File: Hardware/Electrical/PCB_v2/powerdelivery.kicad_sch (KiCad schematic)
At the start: 28 parts, among them J2 USB_C_Receptacle_USB2.0_16P, Q1 Q_PMOS, Q2 Q_PMOS, Q3 Q_PMOS, Q4 Q_PMOS, U2 TPD2EUSB30, U3 CYPD3177-24LQ

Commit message: Components placed
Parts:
- removed C14: 0.1 uF, Capacitor_SMD:C_0603_1608Metric, symbol Device:C
- C10, C13, C8, C9: value 0.1 uF -> 100nF; *LCSC Part Number (none) -> C14663; Manufacturer Würth Elektronik -> (none)
- C11, C12, C6, C7: *LCSC Part Number (none) -> C1848; Manufacturer YAGEO -> (none)
- D2: footprint (none) -> Diode_SMD:D_SOD-323
- J2: Manufacturer SHOU HAN -> (none); now not fitted
- Q1, Q2, Q3, Q4: *LCSC Part Number (none) -> C554002; Manufacturer Vishay Siliconix -> (none)
- R10, R8: footprint (none) -> Resistor_SMD:R_0603_1608Metric; *LCSC Part Number (none) -> C23184
- R11, R12: *LCSC Part Number (none) -> C21190; Manufacturer YAGEO -> (none)
- R13: footprint (none) -> Resistor_SMD:R_0603_1608Metric; *LCSC Part Number (none) -> C23162
- R14, R15, R16, R17: *LCSC Part Number (none) -> C21189; Manufacturer YAGEO -> (none)
- R7: *LCSC Part Number (none) -> C25804; Manufacturer Panasonic Electronic Components -> (none)
- R9: Manufacturer YAGEO -> (none)
- U2: *LCSC Part Number (none) -> C97502; Manufacturer Texas Instruments -> (none)
- U3: *LCSC Part Number (none) -> C2959321

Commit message: PCB finished, export working
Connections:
- net GND: now also J2.SH (SHIELD); no longer J2.S1 (SHIELD)
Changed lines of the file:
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@@
+			)
+		)
+		(property "Manufacturer" ""
+			(at 73.66 87.63 0)
+			(hide yes)
+			(show_name no)
+			(do_not_autoplace no)
+			(effects
+				(font
+					(size 1.27 1.27)
+				)
 			)
 		)
@@
 		(pin "B9"
 		)
-		(pin "S1"
+		(pin "SH"
 		)
 		(pin "A5"

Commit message: first Claude Software
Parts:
- C10, C13, C8, C9: LCSC Part # C6715111 -> C14663
- C11, C12, C6, C7: *LCSC Part Number C1848 -> C15849; LCSC Part # C559769 -> C15849
- J2: LCSC Part # C393939 -> (none)
- R10, R8: LCSC Part # (none) -> C23184
- R11, R12: LCSC Part # C22548 -> C21190
- R13: LCSC Part # (none) -> C23162
- R14, R15, R16, R17: LCSC Part # C95177 -> C21189
- R7: LCSC Part # C161787 -> C25804
- U2: LCSC Part # C94934 -> C97502
- U3: LCSC Part # (none) -> C2959321
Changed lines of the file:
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@@
 			)
 		)
-		(property "LCSC Part #" "C559769"
+		(property "LCSC Part #" "C15849"
 			(at 314.96 77.47 0)
 			(hide yes)
@@
 			)
 		)
-		(property "*LCSC Part Number" "C1848"
+		(property "*LCSC Part Number" "C15849"
 			(at 314.96 77.47 0)
 			(hide yes)
@@
 			)
 		)
-		(property "LCSC Part #" "C6715111"
+		(property "LCSC Part #" "C14663"
 			(at 124.46 78.74 0)
 			(hide yes)
@@
 			)
 		)
-		(property "LCSC Part #" "C559769"
+		(property "LCSC Part #" "C15849"
 			(at 273.05 77.47 0)
 			(hide yes)
@@
 			)
 		)
-		(property "*LCSC Part Number" "C1848"
+		(property "*LCSC Part Number" "C15849"
 			(at 273.05 77.47 0)
 			(hide yes)
@@
 			)
 		)
-		(property "LCSC Part #" "C6715111"
+		(property "LCSC Part #" "C14663"
 			(at 185.42 123.19 0)
 			(hide yes)
@@
 			)
 		)
+		(property "LCSC Part #" "C23184"
+			(at 295.91 77.47 0)
+			(hide yes)
+			(show_name no)
+			(do_not_autoplace no)
+			(effects
+				(font
+					(size 1.27 1.27)
+				)
+			)
+		)
 		(pin "1"
 		)
@@
 			)
 		)
-		(property "LCSC Part #" "C6715111"
+		(property "LCSC Part #" "C14663"
 			(at 113.03 78.74 0)
 			(hide yes)
@@
 			)
 		)
-		(property "LCSC Part #" "C94934"
+		(property "LCSC Part #" "C97502"
 			(at 120.65 100.33 0)
 			(hide yes)
@@
 			)
 		)
-		(property "LCSC Part #" "C22548"
+		(property "LCSC Part #" "C21190"
 			(at 273.05 121.92 90)
 			(hide yes)
@@
 			)
 		)
-		(property "LCSC Part #" "C95177"
+		(property "LCSC Part #" "C21189"
 			(at 177.8 144.78 0)
 			(hide yes)
@@
 			)
 		)
-		(property "LCSC Part #" "C559769"
+		(property "LCSC Part #" "C15849"
 			(at 210.82 123.19 0)
 			(hide yes)
@@
 			)
 		)
-		(property "*LCSC Part Number" "C1848"
+		(property "*LCSC Part Number" "C15849"
 			(at 210.82 123.19 0)
 			(hide yes)
@@
 			)
 		)
-		(property "LCSC Part #" "C95177"
+		(property "LCSC Part #" "C21189"
 			(at 177.8 147.32 0)
 			(hide yes)
@@
 			)
 		)
-		(property "LCSC Part #" "C559769"
+		(property "LCSC Part #" "C15849"
 			(at 193.04 123.19 0)
 			(hide yes)
@@
 			)
 		)
-		(property "*LCSC Part Number" "C1848"
+		(property "*LCSC Part Number" "C15849"
 			(at 193.04 123.19 0)
 			(hide yes)
@@
 			)
 		)
-		(property "LCSC Part #" "C161787"
+		(property "LCSC Part #" "C25804"
 			(at 267.97 77.47 0)
 			(hide yes)
@@
 			)
 		)
-		(property "LCSC Part #" "C393939"
+		(property "LCSC Part #" ""
 			(at 73.66 87.63 0)
 			(hide yes)
@@
 			)
 		)
-		(property "Manufacturer" ""
-			(at 73.66 87.63 0)
-			(hide yes)
-			(show_name no)
-			(do_not_autoplace no)
-			(effects
-				(font
-					(size 1.27 1.27)
-				)
-			)
-		)
 		(pin "B4"
 		)
@@
 			)
 		)
-		(property "LCSC Part #" "C6715111"
+		(property "LCSC Part #" "C14663"
 			(at 218.44 123.19 0)
 			(hide yes)
@@
 			)
 		)
-		(property "LCSC Part #" "C95177"
+		(property "LCSC Part #" "C21189"
 			(at 177.8 162.56 0)
 			(hide yes)
@@
 			)
 		)
-		(property "Manufacturer" ""
-			(at 280.67 74.93 0)
-			(hide yes)
-			(show_name no)
-			(do_not_autoplace no)
-			(effects
-				(font
-					(size 1.27 1.27)
-				)
-			)
-		)
 		(pin "G"
 		)
@@
 			)
 		)
-		(property "LCSC Part #" ""
+		(property "LCSC Part #" "C2959321"
 			(at 201.93 157.48 0)
 			(hide yes)
@@
 			)
 		)
-		(property "Manufacturer" ""
-			(at 292.1 77.47 0)
-			(hide yes)
-			(show_name no)
-			(do_not_autoplace no)
-			(effects
-				(font
-					(size 1.27 1.27)
-				)
-			)
-		)
 		(pin "2"
 		)
@@
 			)
 		)
-		(property "LCSC Part #" "C22548"
+		(property "LCSC Part #" "C21190"
 			(at 297.18 121.92 90)
 			(hide yes)
@@
 			)
 		)
-		(property "LCSC Part #" ""
+		(property "LCSC Part #" "C23162"
 			(at 226.06 139.7 0)
 			(hide yes)
@@
 			)
 		)
-		(property "LCSC Part #" "C95177"
+		(property "LCSC Part #" "C21189"
 			(at 177.8 160.02 0)
 			(hide yes)
@@
 			(at 297.18 99.06 0)
 			(hide yes)
+			(show_name no)
+			(do_not_autoplace no)
+			(effects
+				(font
+					(size 1.27 1.27)
+				)
+			)
+		)
+		(property "LCSC Part #" "C23184"
+			(at 297.18 99.06 0)
+			(hide yes)

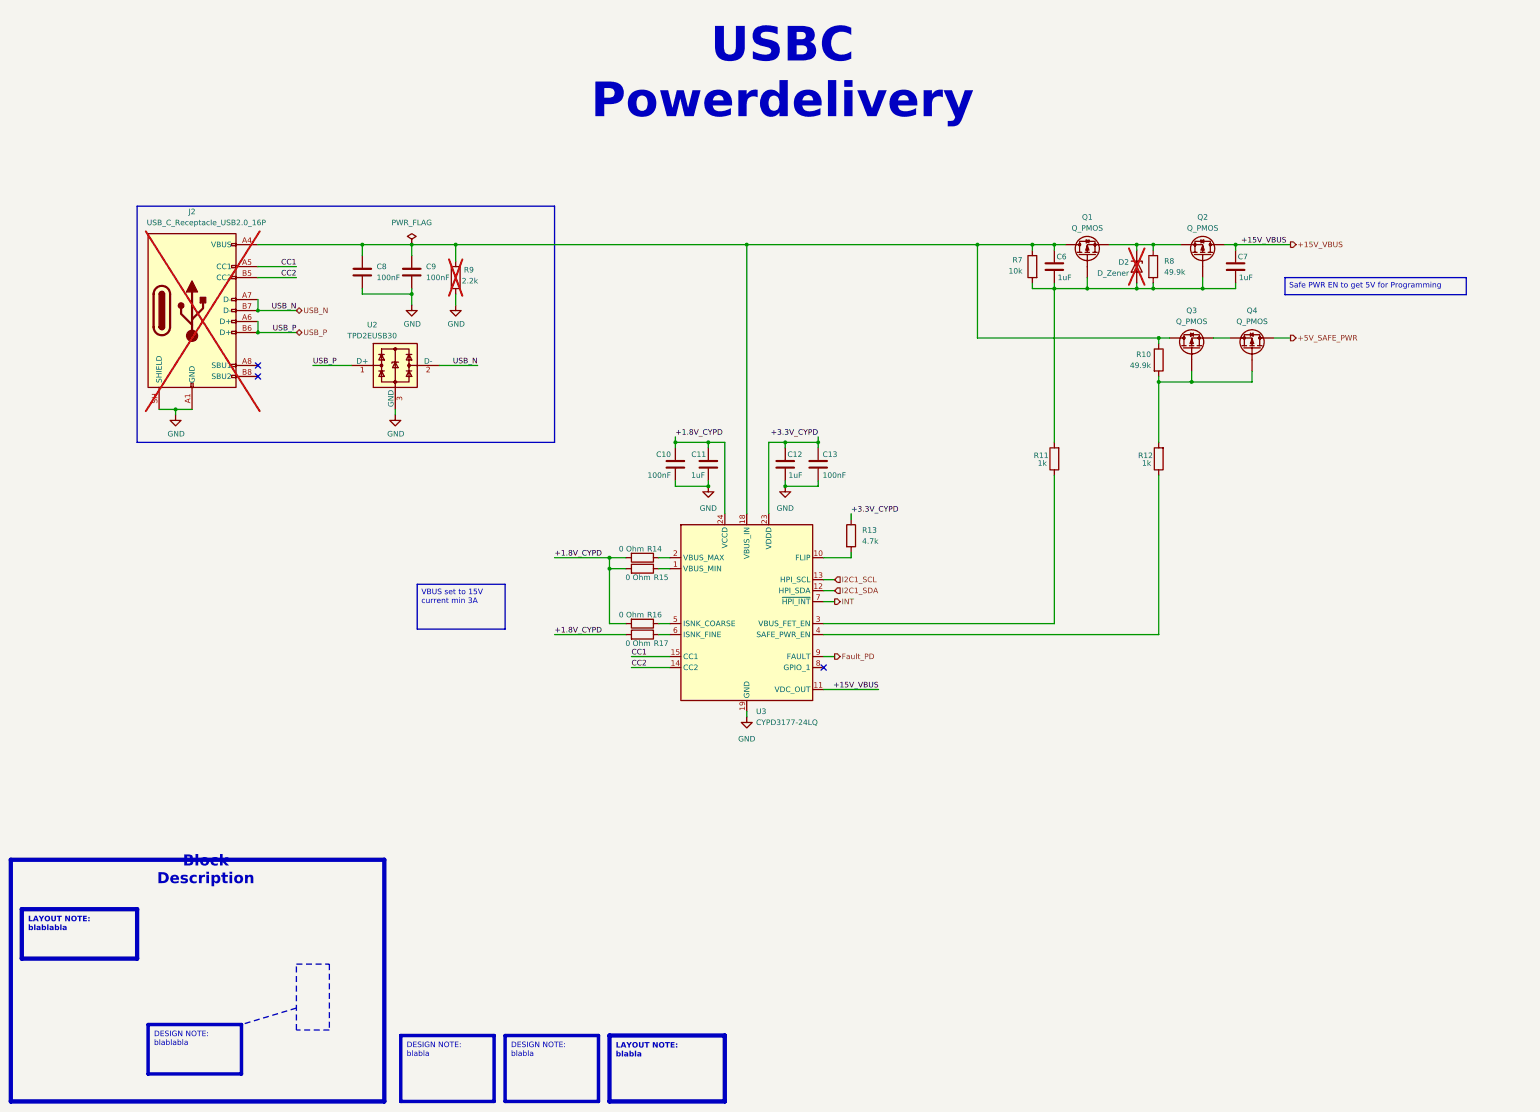
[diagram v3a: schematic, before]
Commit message: first fully working software, undervoltage not added yet
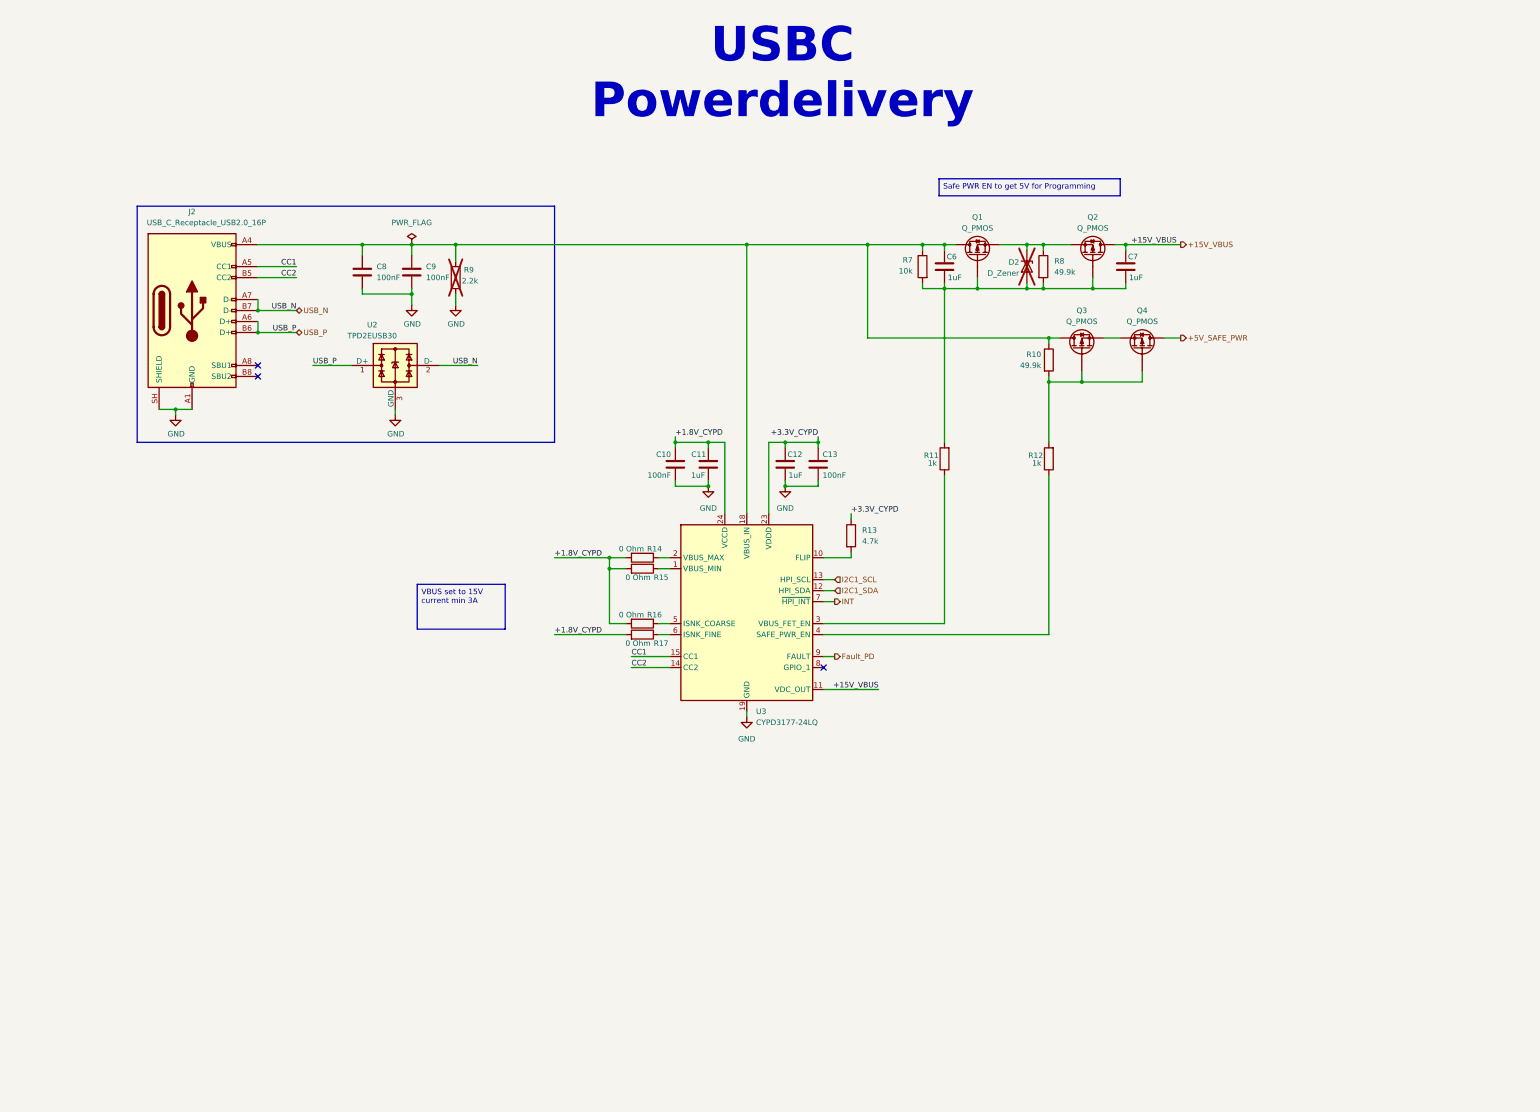
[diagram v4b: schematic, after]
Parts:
- J2: now fitted
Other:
- moved on the sheet: C6, C7, D2, Q1, Q2, Q3, Q4, R10, R11, R12, R7, R8
